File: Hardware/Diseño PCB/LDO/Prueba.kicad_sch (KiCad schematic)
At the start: 57 parts, among them Q1 2N3904, Q10 BC557, Q11 BC547, Q12 BC557, Q13 BC557, Q14 BC547, Q15 BC557, Q16 BC547, Q17 BC557, Q18 BC547, Q19 BC547, Q2 BC547, Q3 BC547, Q4 BC557, Q5 BC557, Q6 BC547, Q7 BC547, Q8 IRF4905, Q9 BC547, U1 TL431LP, U4 LM324

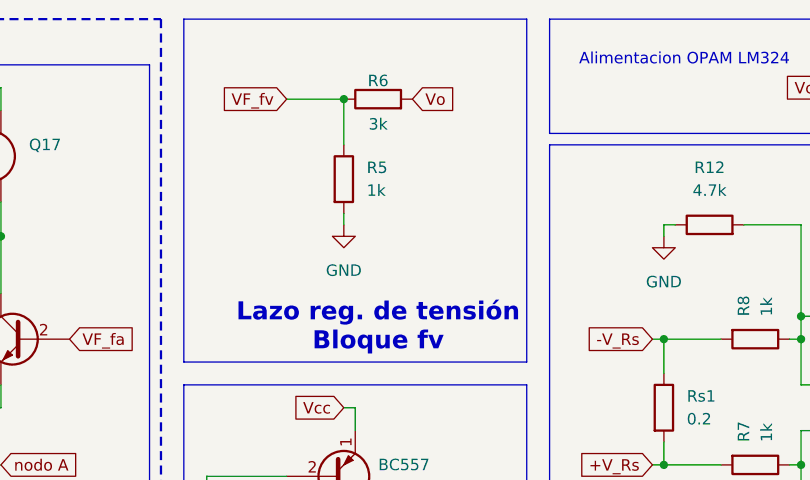
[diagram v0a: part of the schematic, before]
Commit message: Diseño PCB: Correcciones profe y añadi preset
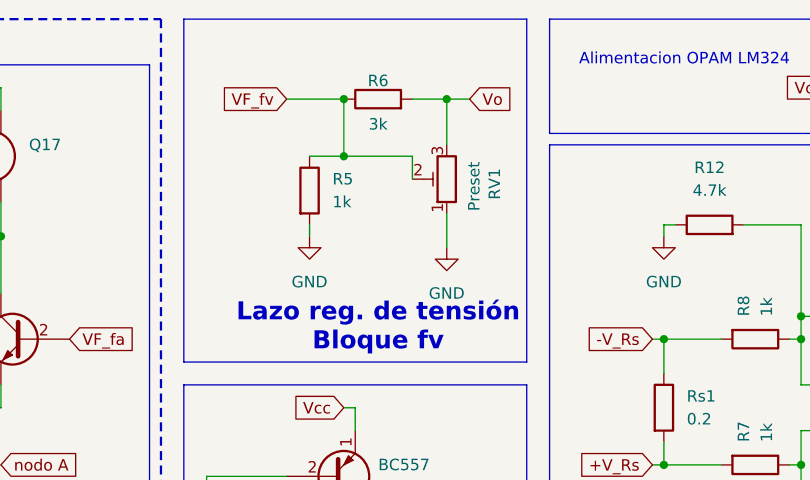
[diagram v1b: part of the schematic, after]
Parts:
- added RV1: Preset, symbol Device:R_Potentiometer_Trim
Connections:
- net -V_Rs: now also RV1.3
- net GND: now also RV1.1
- net VF_fv: now also RV1.2
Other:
- moved on the sheet: R5

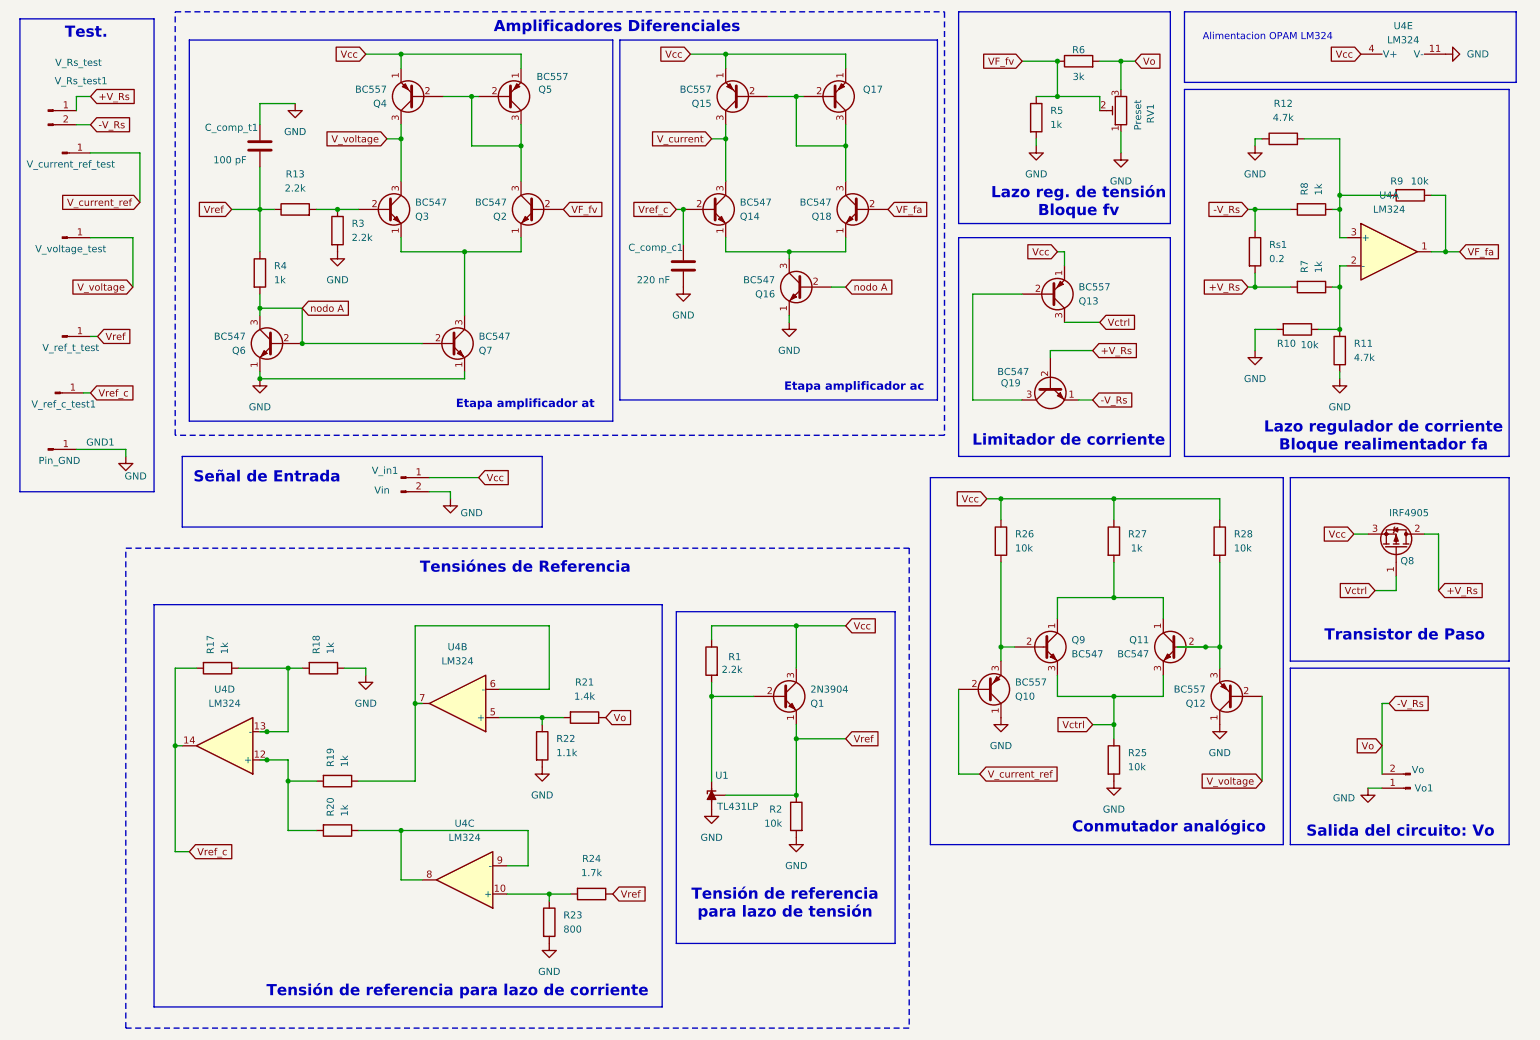
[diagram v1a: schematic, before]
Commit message: Diseño de PCB: Agregue preset lazo de corrente y compensacion de atraso de fase
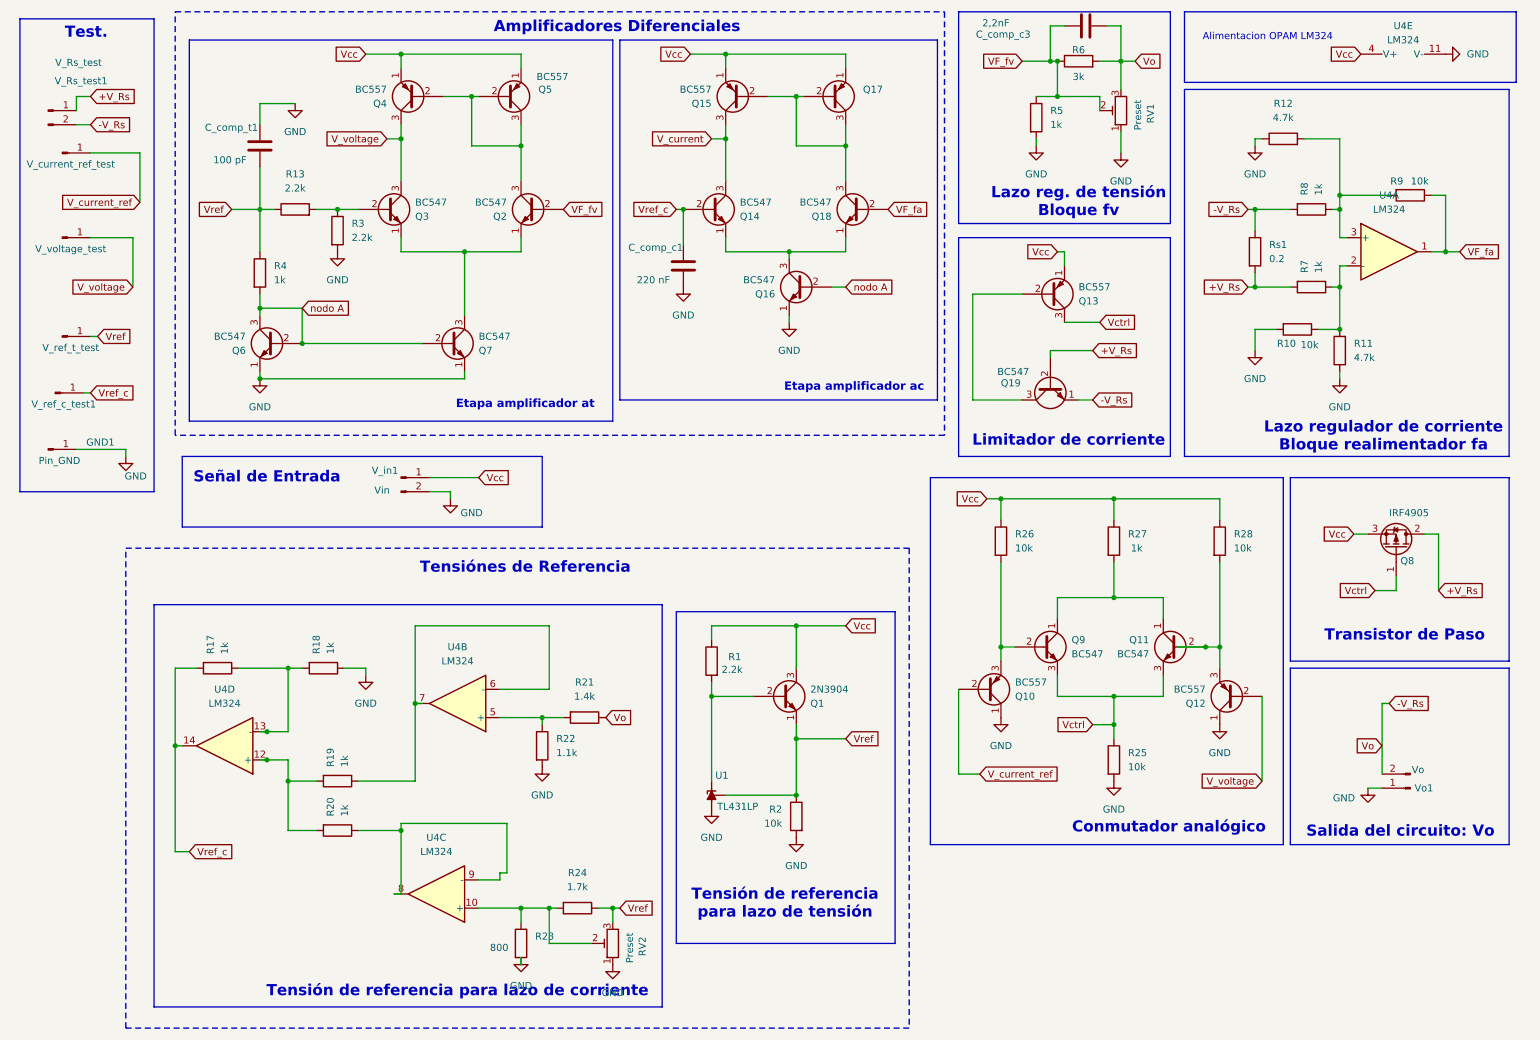
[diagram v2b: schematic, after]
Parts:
- added C_comp_c3: 2,2nF, Capacitor_THT:C_Disc_D3.8mm_W2.6mm_P2.50mm, symbol Device:C
- added RV2: Preset, symbol Device:R_Potentiometer_Trim
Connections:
- net -V_Rs: now also C_comp_c3.2
- net GND: now also RV2.1
- net VF_fv: now also C_comp_c3.1
- net Vref: now also RV2.3
- net at R23.1, R24.2, U4.10 (+): now also RV2.2
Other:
- moved on the sheet: R23, R24, U4C

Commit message: Informe
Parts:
- RV1, RV2: footprint (none) -> Potentiometer_THT:Potentiometer_Bourns_3266W_Vertical
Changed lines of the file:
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@@
 	(wire
 		(pts
+			(xy 276.86 21.59) (xy 270.51 21.59)
+		)
+		(stroke
+			(width 0)
+			(type default)
+		)
+	)
+	(wire
+		(pts
 			(xy 229.87 128.27) (xy 227.33 128.27)
 		)
@@
 	(wire
 		(pts
+			(xy 251.46 21.59) (xy 255.27 21.59)
+		)
+		(stroke
+			(width 0)
+			(type default)
+		)
+	)
+	(wire
+		(pts
 			(xy 251.46 36.83) (xy 251.46 46.99)
 		)
@@
 	(global_label "Vcc"
 		(shape input)
-		(at 255.27 21.59 180)
+		(at 251.46 21.59 180)
 		(fields_autoplaced yes)
 		(effects
@@
 		)
 		(property "Intersheetrefs" "${INTERSHEET_REFS}"
-			(at 249.019 21.59 0)
+			(at 245.209 21.59 0)
 			(hide yes)
 			(show_name no)
@@
 			)
 		)
-		(property "Footprint" ""
+		(property "Footprint" "Potentiometer_THT:Potentiometer_Bourns_3266W_Vertical"
 			(at 120.65 181.61 0)
 			(hide yes)
@@
 	(symbol
 		(lib_id "power:GND")
-		(at 270.51 21.59 90)
+		(at 276.86 21.59 90)
 		(unit 1)
 		(body_style 1)
@@
 		(fields_autoplaced yes)
 		(property "Reference" "#PWR021"
-			(at 276.86 21.59 0)
+			(at 283.21 21.59 0)
 			(hide yes)
 			(show_name no)
@@
 		)
 		(property "Value" "GND"
-			(at 274.32 21.5899 90)
+			(at 280.67 21.5899 90)
 			(show_name no)
 			(do_not_autoplace no)
@@
 		)
 		(property "Footprint" ""
-			(at 270.51 21.59 0)
+			(at 276.86 21.59 0)
 			(hide yes)
 			(show_name no)
@@
 		)
 		(property "Datasheet" ""
-			(at 270.51 21.59 0)
+			(at 276.86 21.59 0)
 			(hide yes)
 			(show_name no)
@@
 		)
 		(property "Description" "Power symbol creates a global label with name \"GND\" , ground"
-			(at 270.51 21.59 0)
+			(at 276.86 21.59 0)
 			(hide yes)
 			(show_name no)
@@
 			)
 		)
-		(property "Footprint" ""
+		(property "Footprint" "Potentiometer_THT:Potentiometer_Bourns_3266W_Vertical"
 			(at 212.09 31.75 0)
 			(hide yes)
